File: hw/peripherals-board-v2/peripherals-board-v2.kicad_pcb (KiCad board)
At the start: 2 copper layers, 75 x 55 mm, 31 parts, among them J1 Screw_Terminal_01x04, J10 RF24, J11 Conn_01x03, J12 Conn_01x03, J13 Conn_01x03, J2 Conn_01x04_Socket, J3 Conn_01x04_Socket, J4 Conn_01x04_Socket, J5 Conn_01x04_Socket, J6 Conn_01x04_Socket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

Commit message: Attempt to rescue schematic
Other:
- board text added: "Board #"
- board text added: "Meat-based drivers are not allowed beyond this point."
- board text added: "Peripherals Interface HW Revision 2"
- board text added: "Status"
- board text removed: "DESIGNED IN KICAD 9 | MANUFACTURED BY ROBU"
- board text removed: "Peripherals Board HW Revision 2"
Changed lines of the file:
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@@
 		)
 	)
-	(gr_text "DESIGNED IN KICAD 9 | MANUFACTURED BY ROBU"
-		(at 106.9 47.3 0)
-		(layer "B.SilkS")
-		(effects
-			(font
-				(size 0.5 0.5)
-				(thickness 0.0625)
-			)
-			(justify left top mirror)
-		)
-	)
-	(gr_text "Peripherals Board\nHW Revision 2"
+	(gr_text "Peripherals Interface\nHW Revision 2"
 		(at 91.2 60.85 0)
 		(layer "B.SilkS")
@@
 		)
 	)
+	(gr_text "Status"
+		(at 76.5 79.1885 0)
+		(layer "B.SilkS")
+		(effects
+			(font
+				(size 0.8 0.8)
+				(thickness 0.1)
+			)
+			(justify top mirror)
+		)
+	)
 	(gr_text "Blogs"
 		(at 47.318929 75.724375 0)
@@
 		)
 	)
+	(gr_text "Meat-based drivers are not allowed beyond this point."
+		(at 97.658932 48.37 0)
+		(layer "B.SilkS")
+		(effects
+			(font
+				(size 1 1)
+				(thickness 0.125)
+			)
+			(justify left top mirror)
+		)
+	)
+	(gr_text "Board #"
+		(at 76.5 71.5185 0)
+		(layer "B.SilkS")
+		(effects
+			(font
+				(size 0.8 0.8)
+				(thickness 0.1)
+			)
+			(justify top mirror)
+		)
+	)
 	(gr_text "Designed by Adbhut Patil\ndiylabsed.github.io/wro-25"
 		(at 91.1 66.1 0)
@@
 		)
 	)
+	(zone
+		(net 0)
+		(net_name "")
+		(layer "B.SilkS")
+		(hatch edge 0.5)
+		(connect_pads
+			(clearance 0.5)
+		)
+		(min_thickness 0.25)
+		(filled_areas_thickness no)
+		(fill yes
+			(thermal_gap 0.5)
+			(thermal_bridge_width 0.5)
+		)
+		(polygon
+			(pts
+				(xy 69.5 80.59) (xy 83.5 80.59) (xy 83.5 85.59) (xy 69.5 85.59)
+			)
+		)
+	)
+	(zone
+		(net 0)
+		(net_name "")
+		(layer "B.SilkS")
+		(hatch edge 0.5)
+		(connect_pads
+			(clearance 0.5)
+		)
+		(min_thickness 0.25)
+		(filled_areas_thickness no)
+		(fill yes
+			(thermal_gap 0.5)
+			(thermal_bridge_width 0.5)
+		)
+		(polygon
+			(pts
+				(xy 79 72.9185) (xy 74 72.9185) (xy 74 77.9185) (xy 79 77.9185)
+			)
+		)
+	)
 	(group ""
 		(members "1f33ba35-fb73-41a0-b711-87afedd66306" "74cd1132-2a3a-4e4e-bb8a-187c3ba843fa"
@@
 	)
 	(group ""
+		(members "bf79ab93-c189-4e06-b075-fc361800eb63")
+	)
+	(group ""
+		(members "54450cf6-3956-4af9-970c-58407cbd09d4" "ffa7acf7-c143-4548-8d59-9e12ae28676b")
+	)
+	(group ""
+		(members "064281cf-0883-4292-900a-1a50879a4f4d" "ed46e547-095f-493e-800a-ab95981a1273")
+	)
+	(group ""
+		(members "94a307c4-3141-4b11-94dd-3b096122225d")
+	)
+	(group ""

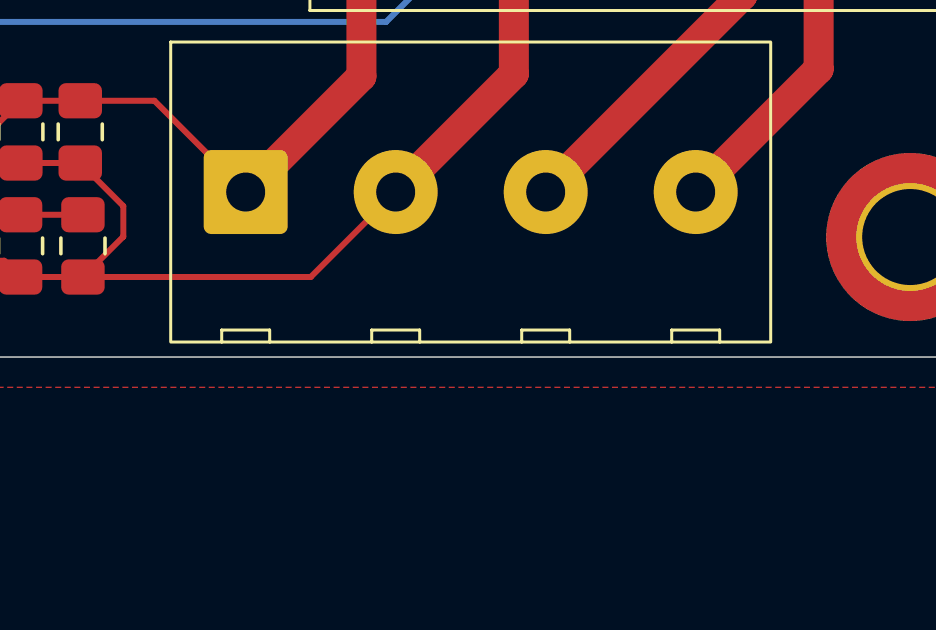
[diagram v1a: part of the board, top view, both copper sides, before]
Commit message: Export gerber files, update interactive BOM
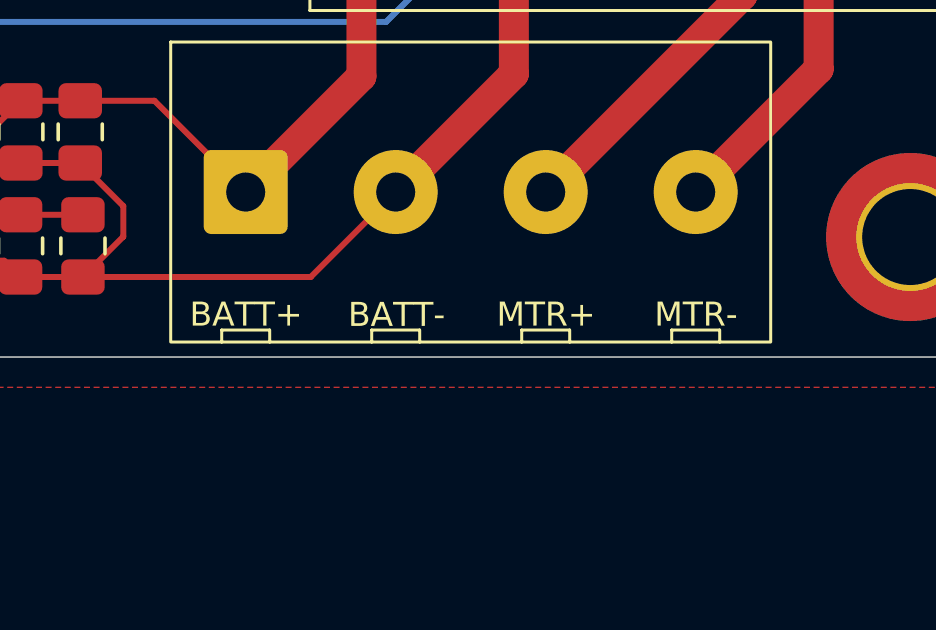
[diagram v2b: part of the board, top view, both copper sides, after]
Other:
- board text added: "BATT+"
- board text added: "BATT-"
- board text added: "MTR+"
- board text added: "MTR-"
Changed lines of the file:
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@@
+		)
+	)
+	(gr_text "MTR-"
+		(at 102.86 101.05 0)
+		(layer "F.SilkS")
+		(effects
+			(font
+				(size 0.8 0.8)
+				(thickness 0.1)
+			)
+			(justify bottom)
 		)
 	)
@@
 			)
 			(justify top)
+		)
+	)
+	(gr_text "BATT-"
+		(at 92.88 101.06 0)
+		(layer "F.SilkS")
+		(effects
+			(font
+				(size 0.8 0.8)
+				(thickness 0.1)
+			)
+			(justify bottom)
 		)
 	)
@@
 		)
 	)
+	(gr_text "BATT+"
+		(at 87.86 101.05 0)
+		(layer "F.SilkS")
+		(effects
+			(font
+				(size 0.8 0.8)
+				(thickness 0.1)
+			)
+			(justify bottom)
+		)
+	)
+	(gr_text "MTR+"
+		(at 97.86 101.05 0)
+		(layer "F.SilkS")
+		(effects
+			(font
+				(size 0.8 0.8)
+				(thickness 0.1)
+			)
+			(justify bottom)
+		)
+	)

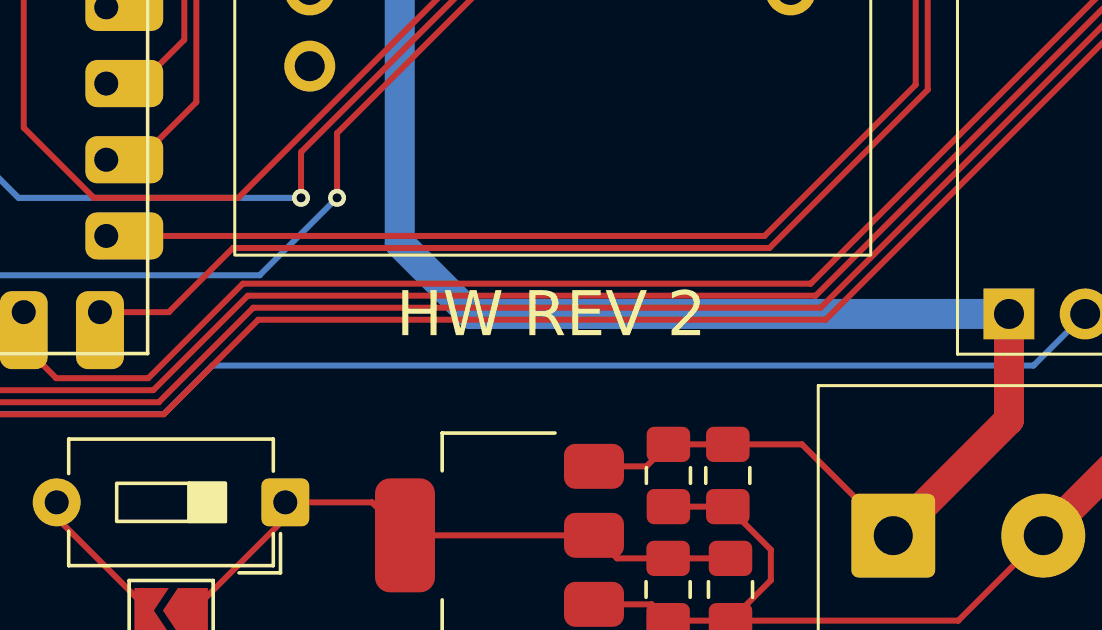
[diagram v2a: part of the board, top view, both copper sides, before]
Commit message: Change silkscreen, regenerate gerber and ibom
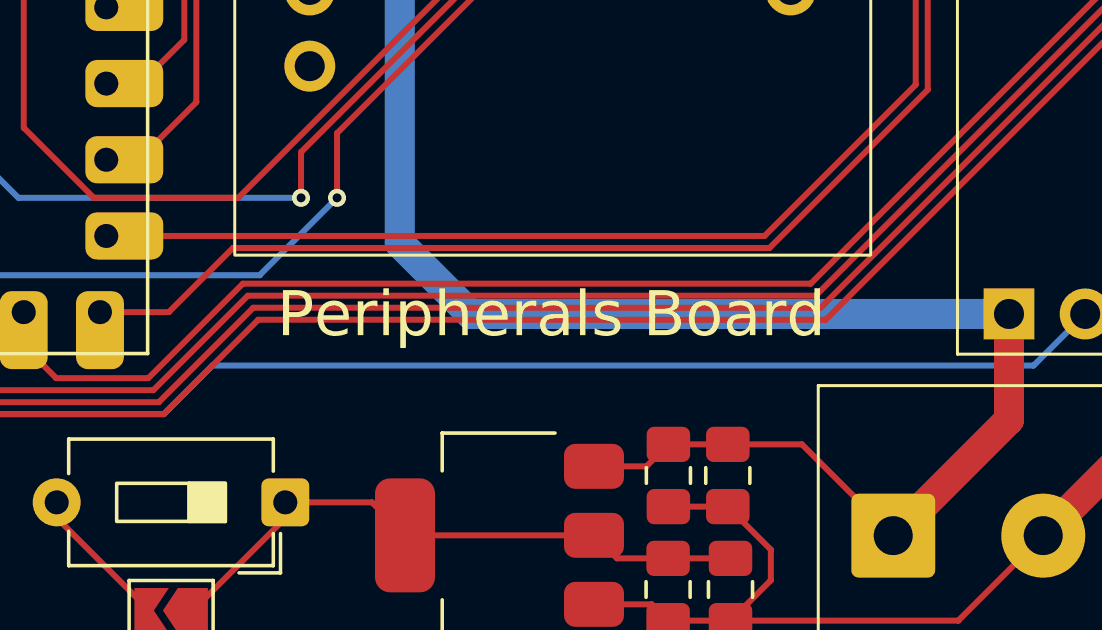
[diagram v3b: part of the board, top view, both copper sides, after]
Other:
- board text added: "Peripherals Board"
- board text removed: "HW REV 2"
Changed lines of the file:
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@@
 		)
 	)
-	(gr_text "HW REV 2"
+	(gr_text "Peripherals Board"
 		(at 76.45 90 0)
 		(layer "F.SilkS")

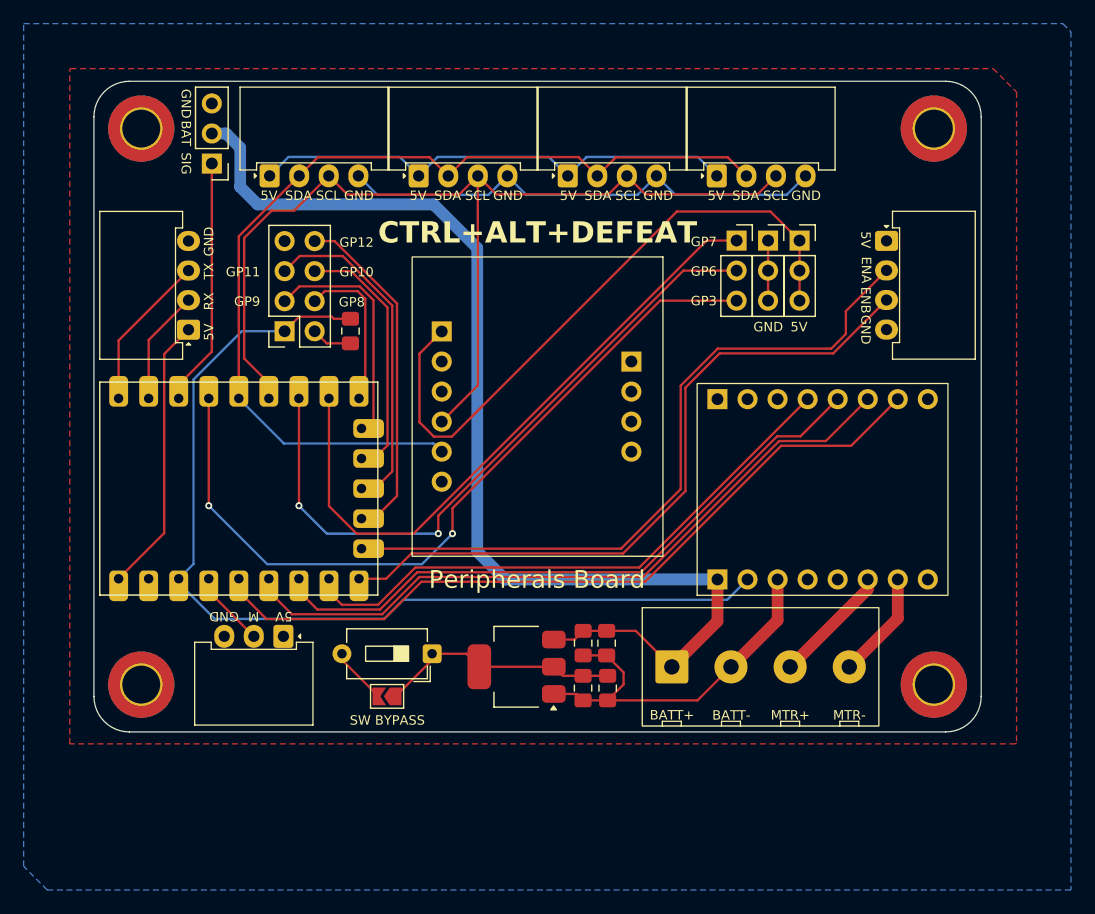
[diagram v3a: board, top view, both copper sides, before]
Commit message: Add reference designators to silkscreen
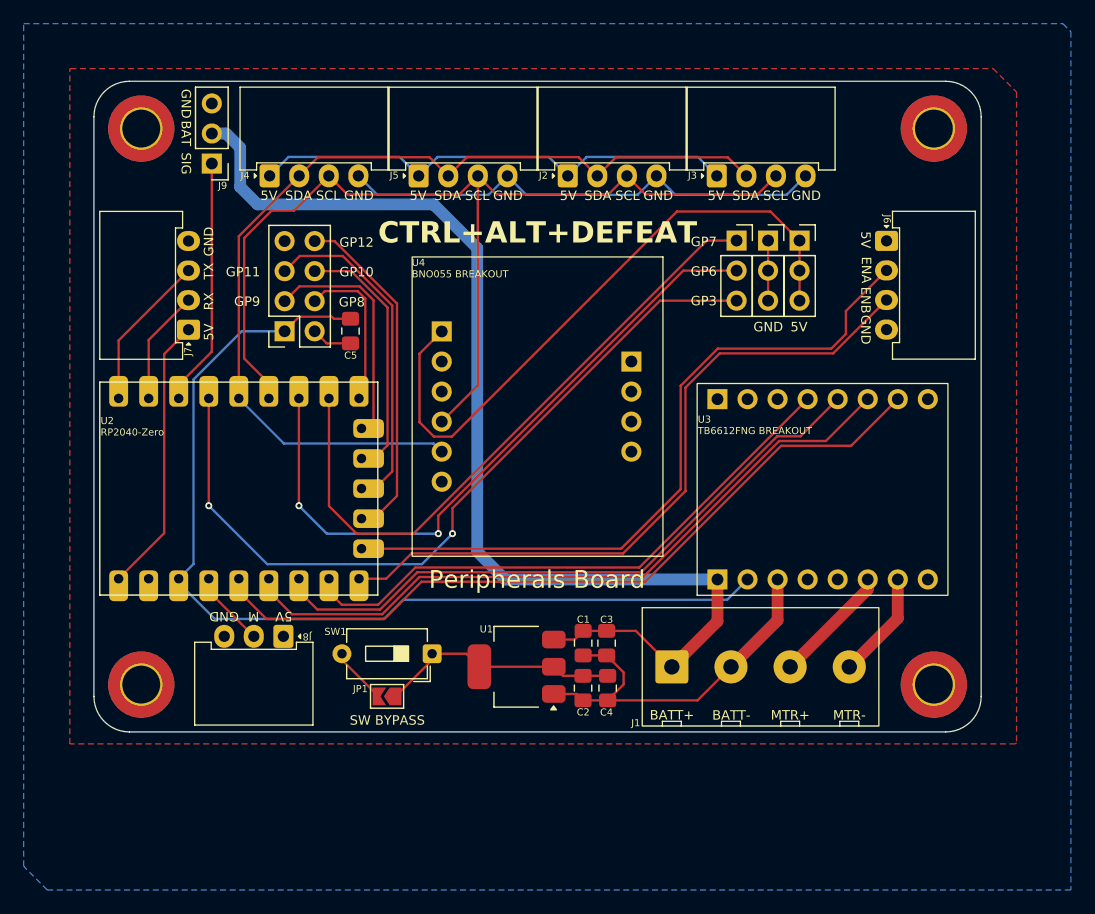
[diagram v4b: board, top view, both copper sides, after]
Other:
- board text added: "C1"
- board text added: "C2"
- board text added: "C3"
- board text added: "C4"
- board text added: "C5"
- board text added: "J1"
- board text added: "J2"
- board text added: "J3"
- board text added: "J4"
- board text added: "J5"
- board text added: "J6"
- board text added: "J7"
- board text added: "J8"
- board text added: "J9"
- board text added: "JP1"
- board text added: "SW1"
- board text added: "U1"
- board text added: "U2 RP2040-Zero"
- board text added: "U3 TB6612FNG BREAKOUT"
- board text added: "U4 BNO055 BREAKOUT"
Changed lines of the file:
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@@
 		(layer "Edge.Cuts")
+	)
+	(gr_text "J5"
+		(at 64.38 54.6 0)
+		(layer "F.SilkS")
+		(effects
+			(font
+				(size 0.6 0.6)
+				(thickness 0.075)
+			)
+			(justify top)
+		)
+	)
+	(gr_text "J8"
+		(at 57.02 94.3 180)
+		(layer "F.SilkS")
+		(effects
+			(font
+				(size 0.6 0.6)
+				(thickness 0.075)
+			)
+			(justify top)
+		)
 	)
 	(gr_text "M"
@@
 		)
 	)
+	(gr_text "C5"
+		(at 60.7 69.82 0)
+		(layer "F.SilkS")
+		(effects
+			(font
+				(size 0.6 0.6)
+				(thickness 0.075)
+			)
+			(justify top)
+		)
+	)
+	(gr_text "J3"
+		(at 89.59 54.61 0)
+		(layer "F.SilkS")
+		(effects
+			(font
+				(size 0.6 0.6)
+				(thickness 0.075)
+			)
+			(justify top)
+		)
+	)
+	(gr_text "J4"
+		(at 51.78 54.61 0)
+		(layer "F.SilkS")
+		(effects
+			(font
+				(size 0.6 0.6)
+				(thickness 0.075)
+			)
+			(justify top)
+		)
+	)
 	(gr_text "GP10"
 		(at 61.2 62.65 0)
@@
 		)
 	)
+	(gr_text "U1"
+		(at 72.17 92.96 0)
+		(layer "F.SilkS")
+		(effects
+			(font
+				(size 0.6 0.6)
+				(thickness 0.075)
+			)
+			(justify top)
+		)
+	)
 	(gr_text "TX"
 		(at 48.25 63.05 90)
@@
 		)
 	)
+	(gr_text "C2"
+		(at 80.36 99.98 0)
+		(layer "F.SilkS")
+		(effects
+			(font
+				(size 0.6 0.6)
+				(thickness 0.075)
+			)
+			(justify top)
+		)
+	)
 	(gr_text "MTR-"
 		(at 102.86 101.05 0)
@@
 		)
 	)
+	(gr_text "J1"
+		(at 84.8 100.89 0)
+		(layer "F.SilkS")
+		(effects
+			(font
+				(size 0.6 0.6)
+				(thickness 0.075)
+			)
+			(justify top)
+		)
+	)
+	(gr_text "J9"
+		(at 49.88 55.47 0)
+		(layer "F.SilkS")
+		(effects
+			(font
+				(size 0.6 0.6)
+				(thickness 0.075)
+			)
+			(justify top)
+		)
+	)
 	(gr_text "GND"
 		(at 96 67.3 0)
@@
 		)
 	)
+	(gr_text "J2"
+		(at 76.99 54.61 0)
+		(layer "F.SilkS")
+		(effects
+			(font
+				(size 0.6 0.6)
+				(thickness 0.075)
+			)
+			(justify top)
+		)
+	)
 	(gr_text "GND"
 		(at 86.7 56.2 0)
@@
 			)
 			(justify top)
+		)
+	)
+	(gr_text "U2\nRP2040-Zero"
+		(at 39.56 75.35 0)
+		(layer "F.SilkS")
+		(effects
+			(font
+				(size 0.6 0.6)
+				(thickness 0.075)
+			)
+			(justify left top)
 		)
 	)
@@
 		)
 	)
+	(gr_text "J6"
+		(at 106.39 58.64 270)
+		(layer "F.SilkS")
+		(effects
+			(font
+				(size 0.6 0.6)
+				(thickness 0.075)
+			)
+			(justify top)
+		)
+	)
 	(gr_text "SCL"
 		(at 71.4 56.2 0)
@@
 		)
 	)
+	(gr_text "C1"
+		(at 80.37 92.14 0)
+		(layer "F.SilkS")
+		(effects
+			(font
+				(size 0.6 0.6)
+				(thickness 0.075)
+			)
+			(justify top)
+		)
+	)
 	(gr_text "SDA"
 		(at 94.1 56.2 0)
@@
 		)
 	)
+	(gr_text "U4\nBNO055 BREAKOUT"
+		(at 65.87 61.98 0)
+		(layer "F.SilkS")
+		(effects
+			(font
+				(size 0.6 0.6)
+				(thickness 0.075)
+			)
+			(justify left top)
+		)
+	)
 	(gr_text "RX"
 		(at 48.25 65.6 90)
@@
 		)
 	)
+	(gr_text "C3"
+		(at 82.34 92.15 0)
+		(layer "F.SilkS")
+		(effects
+			(font
+				(size 0.6 0.6)
+				(thickness 0.075)
+			)
+			(justify top)
+		)
+	)
 	(gr_text "BATT+"
 		(at 87.86 101.05 0)
@@
 		)
 	)
+	(gr_text "U3\nTB6612FNG BREAKOUT"
+		(at 90.04 75.23 0)
+		(layer "F.SilkS")
+		(effects
+			(font
+				(size 0.6 0.6)
+				(thickness 0.075)
+			)
+			(justify left top)
+		)
+	)
+	(gr_text "SW1"
+		(at 59.41 93.17 0)
+		(layer "F.SilkS")
+		(effects
+			(font
+				(size 0.6 0.6)
+				(thickness 0.075)
+			)
+			(justify top)
+		)
+	)
 	(gr_text "GND"
 		(at 50 92.7 180)
@@
 		)
 	)
+	(gr_text "J7"
+		(at 46.61 69.84 90)
+		(layer "F.SilkS")
+		(effects
+			(font
+				(size 0.6 0.6)
+				(thickness 0.075)
+			)
+			(justify top)
+		)
+	)
 	(gr_text "GP3"
 		(at 90.55 65.1 0)
@@
 		)
 	)
+	(gr_text "C4"
+		(at 82.33 99.99 0)
+		(layer "F.SilkS")
+		(effects
+			(font
+				(size 0.6 0.6)
+				(thickness 0.075)
+			)
+			(justify top)
+		)
+	)
 	(gr_text "GP9"
 		(at 51.95 65.15 0)
@@
 			)
 			(justify top)
+		)
+	)
+	(gr_text "JP1"
+		(at 61.52 98.01 0)
+		(layer "F.SilkS")
+		(effects
+			(font
+				(size 0.6 0.6)
+				(thickness 0.075)
+			)
+			(justify top)
